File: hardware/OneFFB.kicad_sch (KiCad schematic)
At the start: 2 parts

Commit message: finish power tree
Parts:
- added C?: 1n, symbol Device:C_Small
- added C? (x3): 100n, symbol Device:C_Small
- added J?: Conn_01x03_Female, symbol Connector:Conn_01x03_Female
- added Q? (x6): CSD18540Q5B, Package_TO_SOT_SMD:TDSON-8-1, symbol Transistor_FET:CSD18540Q5B
- added R? (x2): 3m, symbol Device:R_Small
- added U?: AD8418, symbol Amplifier_Current:AD8418
- added U? (x3): LM5109BSD, Package_SON:WSON-8-1EP_4x4mm_P0.8mm_EP2.6x3mm, symbol Driver_FET:LM5109BSD
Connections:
- net GND: now also C?.2, Q?.1 (S), Q?.1 (S), Q?.1 (S), Q?.2 (S), Q?.2 (S), Q?.2 (S), Q?.3 (S), Q?.3 (S), Q?.3 (S), U?.2 (GND)
- new net: R?.2, U?.1 (IN-)
- new net: C?.1, U?.5 (OUT)
- new net: Q?.1 (S), Q?.2 (S), Q?.3 (S), Q?.5 (D), R?.1, U?.6 (HS), U?.8 (IN+)
- new net: C?.1, U?.8 (HB) (x3)
- new net: C?.2, Q?.4 (G), U?.7 (HO) (x3)
- new net: Q?.4 (G), U?.5 (LO) (x3)
- new net: Q?.1 (S), Q?.2 (S), Q?.3 (S), Q?.5 (D), U?.6 (HS) (x2)
- new net: Q?.5 (D), Q?.5 (D), Q?.5 (D)
- new net: U?.4 (VSS), U?.9 (VSS) (x3)
- new net +5V: U?.6 (VS)
- new net HI1: U?.2 (HI)
- new net HI2: U?.2 (HI)
- new net HI3: U?.2 (HI)
- new net LI1: U?.3 (LI)
- new net LI2: U?.3 (LI)
- new net LI3: U?.3 (LI)
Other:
- sheet power ports: added +10V, +3V3, +5V, VBUS; removed none
- note added: "3 phase half bridge"
- moved on the sheet: U?

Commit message: add motor sch, move gate driver to motor sch
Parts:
- removed C?: 1n, symbol Device:C_Small
- removed C? (x3): 100n, symbol Device:C_Small
- removed J?: Conn_01x03_Female, symbol Connector:Conn_01x03_Female
- removed Q? (x6): CSD18540Q5B, Package_TO_SOT_SMD:TDSON-8-1, symbol Transistor_FET:CSD18540Q5B
- removed R? (x2): 3m, symbol Device:R_Small
- removed U?: AD8418, symbol Amplifier_Current:AD8418
- removed U? (x3): LM5109BSD, Package_SON:WSON-8-1EP_4x4mm_P0.8mm_EP2.6x3mm, symbol Driver_FET:LM5109BSD
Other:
- added sheet motor_driver (motor_driver.kicad_sch)
- note removed: "3 phase half bridge"

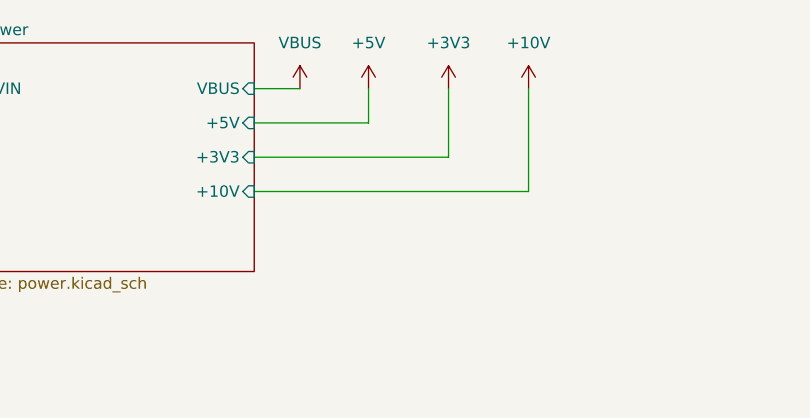
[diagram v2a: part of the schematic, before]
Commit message: add 1.8v LDO for TMC4671 core
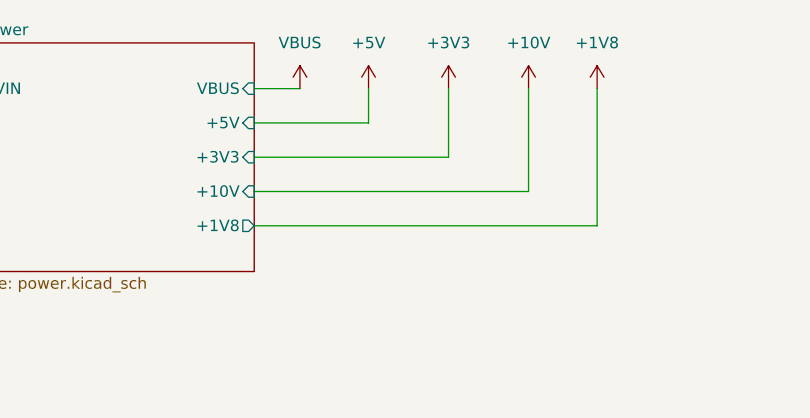
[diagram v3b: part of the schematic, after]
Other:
- sheet power ports: added +1V8; removed none
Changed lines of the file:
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@@
+    (stroke (width 0) (type default) (color 0 0 0 0))
+  )
+  (wire (pts (xy 115.57 30.48) (xy 115.57 45.72))
     (stroke (width 0) (type default) (color 0 0 0 0))
   )
   (wire (pts (xy 38.1 35.56) (xy 34.29 35.56))
+    (stroke (width 0) (type default) (color 0 0 0 0))
+  )
+  (wire (pts (xy 77.47 45.72) (xy 115.57 45.72))
     (stroke (width 0) (type default) (color 0 0 0 0))
   )
@@
     (pin "1")
   )
+  (symbol (lib_id "power:+1V8") (at 115.57 30.48 0) (unit 1)
+    (in_bom yes) (on_board yes) (fields_autoplaced)
+    (property "Reference" "#PWR?" (id 0) (at 115.57 34.29 0)
+      (effects (font (size 1.27 1.27)) hide)
+    )
+    (property "Value" "+1V8" (id 1) (at 115.57 25.4 0))
+    (property "Footprint" "" (id 2) (at 115.57 30.48 0)
+      (effects (font (size 1.27 1.27)) hide)
+    )
+    (property "Datasheet" "" (id 3) (at 115.57 30.48 0)
+      (effects (font (size 1.27 1.27)) hide)
+    )
+    (pin "1")
+  )
   (symbol (lib_id "power:+5V") (at 90.17 30.48 0) (unit 1)
     (in_bom yes) (on_board yes) (fields_autoplaced)
@@
       (effects (font (size 1.27 1.27)) (justify right))
     )
+    (pin "+1V8" output (at 77.47 45.72 0)
+      (effects (font (size 1.27 1.27)) (justify right))
+    )
   )
   (sheet (at 158.75 34.29) (size 86.36 59.69) (fields_autoplaced)
@@
       (reference "#PWR?") (unit 1) (value "GND") (footprint "")
     )
+    (path "/63a52cb1-2fe5-4fa7-925d-569298fff5a6/0e5fe037-2cac-4186-9536-9295838577e0"
+      (reference "#PWR?") (unit 1) (value "GND") (footprint "")
+    )
+    (path "/63a52cb1-2fe5-4fa7-925d-569298fff5a6/10f2abcd-c143-4ea4-b5b8-d04515818a8b"
+      (reference "#PWR?") (unit 1) (value "GND") (footprint "")
+    )
     (path "/1342daf5-6a6b-41a4-84c5-c55f7a7a35bd"
       (reference "#PWR?") (unit 1) (value "+10V") (footprint "")
     )
+    (path "/2361ddb3-5d21-448c-b657-34d39f7d950a"
+      (reference "#PWR?") (unit 1) (value "+1V8") (footprint "")
+    )
     (path "/09603403-8b22-4930-9b39-39c13f819f7b/2a212e20-deaf-4162-9ff3-be34dbbb2d94"
       (reference "#PWR?") (unit 1) (value "GND") (footprint "")
@@
     (path "/09603403-8b22-4930-9b39-39c13f819f7b/4f88e9f3-3a4c-400a-bdba-73b234f6dfb5"
       (reference "#PWR?") (unit 1) (value "GND") (footprint "")
+    )
+    (path "/63a52cb1-2fe5-4fa7-925d-569298fff5a6/5c8074eb-b699-437f-9f9a-b7d6f0379726"
+      (reference "#PWR?") (unit 1) (value "GND") (footprint "")
+    )
+    (path "/63a52cb1-2fe5-4fa7-925d-569298fff5a6/62c2efd9-2929-4749-989c-66390250d7ff"
+      (reference "#PWR?") (unit 1) (value "+5V") (footprint "")
     )
     (path "/649d85b9-5562-457c-8f86-98dbf246f99b"
@@
       (reference "#PWR?") (unit 1) (value "GND") (footprint "")
     )
+    (path "/09603403-8b22-4930-9b39-39c13f819f7b/8d0d3cd9-9da2-426c-95de-fc3d5062ba97"
+      (reference "#PWR?") (unit 1) (value "GND") (footprint "")
+    )
     (path "/63a52cb1-2fe5-4fa7-925d-569298fff5a6/911ad197-d869-4a7f-ad5d-2603f87ceb8a"
       (reference "#PWR?") (unit 1) (value "GND") (footprint "")
     )
+    (path "/63a52cb1-2fe5-4fa7-925d-569298fff5a6/9f3cb56e-8c18-4cfa-9b25-9b81a6014e4c"
+      (reference "#PWR?") (unit 1) (value "+3V3") (footprint "")
+    )
     (path "/63a52cb1-2fe5-4fa7-925d-569298fff5a6/a59b610f-c09a-42fa-959b-c0c2709cfa54"
       (reference "#PWR?") (unit 1) (value "GND") (footprint "")
     )
     (path "/09603403-8b22-4930-9b39-39c13f819f7b/b89425be-5318-4343-8b43-679c9d9ed507"
+      (reference "#PWR?") (unit 1) (value "GND") (footprint "")
+    )
+    (path "/09603403-8b22-4930-9b39-39c13f819f7b/c3d24cfa-7f19-4801-91c2-0104d516db38"
       (reference "#PWR?") (unit 1) (value "GND") (footprint "")
     )
@@
       (reference "#PWR?") (unit 1) (value "+5V") (footprint "")
     )
+    (path "/63a52cb1-2fe5-4fa7-925d-569298fff5a6/e3656fa1-eca0-442d-b665-3fee17dae2de"
+      (reference "#PWR?") (unit 1) (value "+1V8") (footprint "")
+    )
     (path "/09603403-8b22-4930-9b39-39c13f819f7b/e5132e66-6cc5-41fc-a9e0-aba746a4502c"
       (reference "#PWR?") (unit 1) (value "GND") (footprint "")
@@
       (reference "#PWR?") (unit 1) (value "+3V3") (footprint "")
     )
+    (path "/09603403-8b22-4930-9b39-39c13f819f7b/e7593b06-b8bc-4cd9-8175-3318f0857ad6"
+      (reference "#PWR?") (unit 1) (value "GND") (footprint "")
+    )
     (path "/09603403-8b22-4930-9b39-39c13f819f7b/f21e2a07-4a3e-40c8-8df4-f9c3a6efc7c2"
       (reference "#PWR?") (unit 1) (value "GND") (footprint "")
@@
       (reference "C?") (unit 1) (value "1u") (footprint "")
     )
+    (path "/63a52cb1-2fe5-4fa7-925d-569298fff5a6/258c87a1-5ebf-4ef8-bb1f-9480a5603adb"
+      (reference "C?") (unit 1) (value "100n") (footprint "")
+    )
+    (path "/63a52cb1-2fe5-4fa7-925d-569298fff5a6/2cd99076-9f9f-4014-b3a9-1d186c3e6c82"
+      (reference "C?") (unit 1) (value "100n") (footprint "")
+    )
+    (path "/63a52cb1-2fe5-4fa7-925d-569298fff5a6/32bb6d6f-6acf-4028-92dc-da48b27b2ac8"
+      (reference "C?") (unit 1) (value "100n") (footprint "")
+    )
     (path "/09603403-8b22-4930-9b39-39c13f819f7b/336f1d5f-55c9-4180-9437-fc7e36dfe154"
       (reference "C?") (unit 1) (value "220uF") (footprint "")
@@
       (reference "C?") (unit 1) (value "220uF") (footprint "")
     )
+    (path "/63a52cb1-2fe5-4fa7-925d-569298fff5a6/468ac077-ac46-43eb-895e-bb76652e0671"
+      (reference "C?") (unit 1) (value "100n") (footprint "")
+    )
     (path "/09603403-8b22-4930-9b39-39c13f819f7b/4ed6a7a2-836b-4610-8d7b-79456e2ee453"
       (reference "C?") (unit 1) (value "22u") (footprint "")
@@
       (reference "C?") (unit 1) (value "330p") (footprint "")
     )
+    (path "/63a52cb1-2fe5-4fa7-925d-569298fff5a6/5788f6ee-a950-4b1b-aaa9-d2665c0c4242"
+      (reference "C?") (unit 1) (value "100n") (footprint "")
+    )
     (path "/09603403-8b22-4930-9b39-39c13f819f7b/57a762d4-1a7c-46c8-9ff8-3756d3021a0f"
       (reference "C?") (unit 1) (value "220uF") (footprint "")
@@
       (reference "C?") (unit 1) (value "1u") (footprint "")
     )
+    (path "/63a52cb1-2fe5-4fa7-925d-569298fff5a6/6ee75561-ce84-4a22-bee2-e6de9eaa71cb"
+      (reference "C?") (unit 1) (value "10u") (footprint "")
+    )
+    (path "/09603403-8b22-4930-9b39-39c13f819f7b/72de813e-dd4a-46b8-b6b0-ca578da75b41"
+      (reference "C?") (unit 1) (value "1u") (footprint "")
+    )
+    (path "/63a52cb1-2fe5-4fa7-925d-569298fff5a6/73d050ef-f762-4ee7-9a74-1bdbcc45a8b9"
+      (reference "C?") (unit 1) (value "100n") (footprint "")
+    )
     (path "/63a52cb1-2fe5-4fa7-925d-569298fff5a6/79c3dc4e-788d-45ec-a532-9865e9ed5f4c"
       (reference "C?") (unit 1) (value "100n") (footprint "")
@@
       (reference "C?") (unit 1) (value "1u") (footprint "")
     )
+    (path "/09603403-8b22-4930-9b39-39c13f819f7b/87e8328e-e937-4281-9a1d-c42173991c80"
+      (reference "C?") (unit 1) (value "1u") (footprint "")
+    )
     (path "/09603403-8b22-4930-9b39-39c13f819f7b/93ff17c7-2369-4f11-8f1c-fafd7d4ee716"
       (reference "C?") (unit 1) (value "10u") (footprint "")
@@
       (reference "C?") (unit 1) (value "33u") (footprint "")
     )
+    (path "/63a52cb1-2fe5-4fa7-925d-569298fff5a6/ad478d26-a9cc-4a91-bf0f-216be07cfc43"
+      (reference "C?") (unit 1) (value "100n") (footprint "")
+    )
     (path "/09603403-8b22-4930-9b39-39c13f819f7b/b41b2ff5-707e-4461-b023-160638cc9e7f"
       (reference "C?") (unit 1) (value "10u") (footprint "")
@@
       (reference "C?") (unit 1) (value "100n") (footprint "")
     )
+    (path "/63a52cb1-2fe5-4fa7-925d-569298fff5a6/b71e57a1-0d6f-4aaa-b359-d9045f57a188"
+      (reference "C?") (unit 1) (value "100n") (footprint "")
+    )
+    (path "/63a52cb1-2fe5-4fa7-925d-569298fff5a6/b99072e0-4e94-4867-a3d0-c42fe81863a0"
+      (reference "C?") (unit 1) (value "100n") (footprint "")
+    )
     (path "/09603403-8b22-4930-9b39-39c13f819f7b/b5d4c71d-b741-4102-b3c3-01709a5ec798"
       (reference "D?") (unit 1) (value "SS34") (footprint "Diode_THT:D_DO-35_SOD27_P7.62mm_Horizontal")
@@
       (reference "U?") (unit 1) (value "STM32F411CEUx") (footprint "Package_DFN_QFN:QFN-48-1EP_7x7mm_P0.5mm_EP5.6x5.6mm")
     )
+    (path "/63a52cb1-2fe5-4fa7-925d-569298fff5a6/2a396d2f-1519-47b1-a6f7-3489c517a4a7"
+      (reference "U?") (unit 1) (value "TMC4671-LA") (footprint "Package_DFN_QFN:QFN-76-1EP_11.5x6.5mm_P0.4_EP9x5mm")
+    )
     (path "/09603403-8b22-4930-9b39-39c13f819f7b/38324222-ebdd-4e06-abe7-ddc1210fdee3"
       (reference "U?") (unit 1) (value "MT3608") (footprint "Package_TO_SOT_SMD:SOT-23-6")
@@
       (reference "U?") (unit 1) (value "LM5109BSD") (footprint "Package_SON:WSON-8-1EP_4x4mm_P0.8mm_EP2.6x3mm")
     )
+    (path "/09603403-8b22-4930-9b39-39c13f819f7b/564880a2-38ad-4e1d-a994-3dfba276d2e5"
+      (reference "U?") (unit 1) (value "AMS1117-1.8") (footprint "Package_TO_SOT_SMD:SOT-223-3_TabPin2")
+    )
     (path "/63a52cb1-2fe5-4fa7-925d-569298fff5a6/a4310579-561e-4b24-9b68-0c28192570f7"

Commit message: add firmware
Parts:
- added C1: 4.7u, Capacitor_SMD:C_0402_1005Metric, symbol Device:C_Small
- added C10, C4, C5, C6, C7, C8: 100n, Capacitor_SMD:C_0402_1005Metric, symbol Device:C_Small
- added C11, C9: 1u, Capacitor_SMD:C_0402_1005Metric, symbol Device:C_Small
- added C2, C3: 15p, Capacitor_SMD:C_0402_1005Metric, symbol Device:C_Small
- added J1: USB_B_Mini, symbol Connector:USB_B_Mini
- added J3: DEBUG, symbol Connector:Conn_01x03_Female
- added J4: Encoder, symbol Connector:Conn_01x05_Male
- added R1, R4: 10k, symbol Device:R_Small
- added R2, R3: 22r, symbol Device:R_Small
- added SW1: SW_Push, symbol Switch:SW_Push
- added U2: 74LVC3G34, symbol 74xGxx:74LVC3G34
- added Y1: 8M, symbol Device:Crystal_Small
- gave numbers to parts that had none: 2
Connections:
- net +3V3: now also U1.1 (VBAT), U1.24 (VDD), U1.36 (VDD), U1.48 (VDD), U1.9 (VDDA), C11.1, C4.1, C5.1, C6.1, C7.1, C8.1, C9.1, J4.1 (Pin_1), R4.2, U2.8 (VCC), U2.8 (VCC), U2.8 (VCC)
- net GND: now also U1.23 (VSS), U1.35 (VSS), U1.47 (VSS), U1.49 (VSS), U1.8 (VSSA), C1.2, C11.2, C2.2, C3.2, C4.2, C5.2, C6.2, C7.2, C8.2, C9.2, J1.5 (GND), J1.6 (Shield), J3.3 (Pin_3), J4.5 (Pin_5), R1.2, U2.4 (GND), U2.4 (GND), U2.4 (GND)
- net DRV_STATUS: now reaches U1.12 (PA2)
- net SPI_NSS: now reaches U1.14 (PA4)
- net SPI_SCK: now reaches U1.15 (PA5)
- net SPI_MISO: now reaches U1.16 (PA6)
- net SPI_MOSI: now reaches U1.17 (PA7)
- net at U1.22 (VCAP1): now also C1.1
- net ENC_A: now reaches U1.29 (PA8)
- net ENC_A: now also U2.7
- net ENC_B: now reaches U1.30 (PA9)
- net ENC_B: now also U2.2
- net ENC_N: now reaches U1.31 (PA10)
- net ENC_N: now also U2.5
- net USB_D-: now reaches U1.32 (PA11)
- net USB_D-: now also R3.2
- net USB_D+: now reaches U1.33 (PA12)
- net USB_D+: now also R2.2
- net at U1.34 (PA13): now also J3.1 (Pin_1)
- net at U1.37 (PA14): now also J3.2 (Pin_2)
- net at U1.44 (BOOT0): now also R1.1
- net at U1.5 (PH0): now also C2.1, Y1.1
- net at U1.6 (PH1): now also C3.1, Y1.2
- net NRST: now reaches U1.7 (NRST)
- net NRST: now also C10.2, SW1.2
- new net: C10.1, R4.1, SW1.1
- new net: J4.2 (Pin_2), U2.1
- new net: J1.2 (D-), R3.1
- new net: J1.3 (D+), R2.1
- new net: J4.3 (Pin_3), U2.6
- new net: J4.4 (Pin_4), U2.3
- no-connect marks 0 -> 24
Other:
- sheet motor_driver ports: added DRV_ENABLE, DRV_ENC_A, DRV_ENC_B, DRV_ENC_N, DRV_NRST, DRV_SPI_CS, DRV_SPI_MISO, DRV_SPI_MOSI, DRV_SPI_SCK, DRV_STATUS; removed none
